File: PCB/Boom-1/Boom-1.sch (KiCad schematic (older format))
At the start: 702 parts

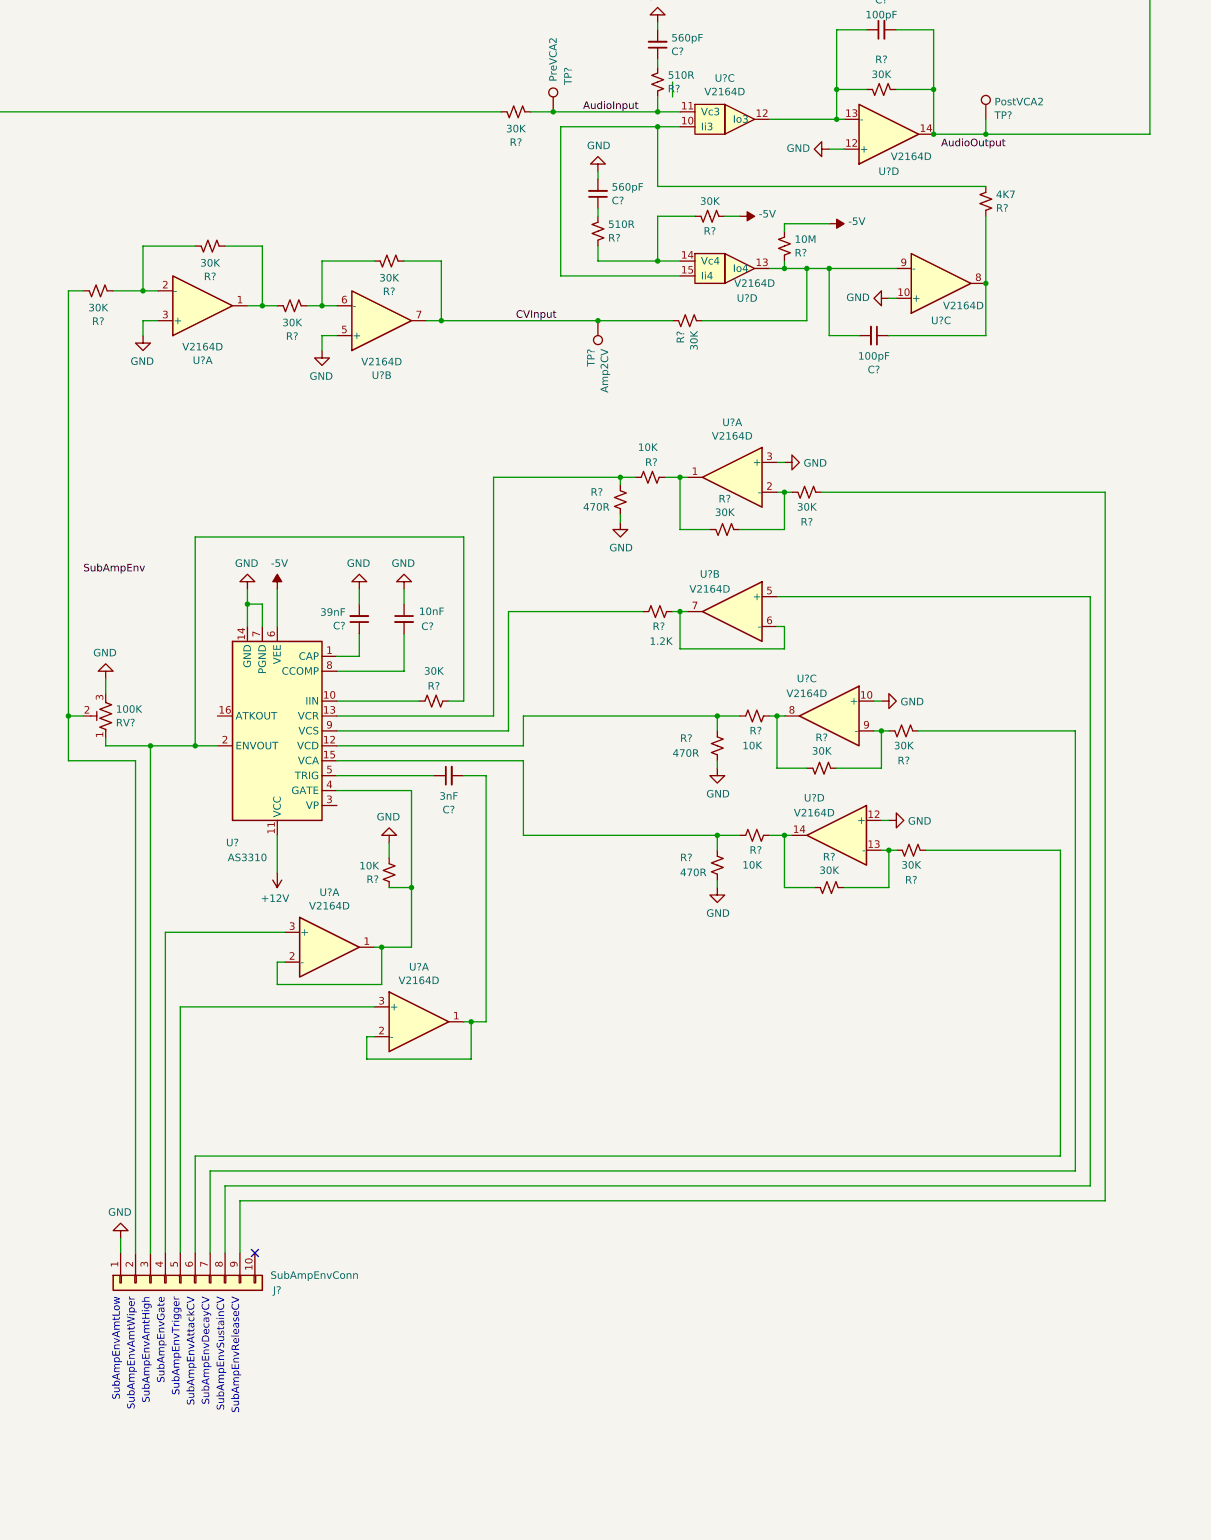
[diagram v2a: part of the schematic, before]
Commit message: replaced tl074 and tl072s in sub osc amp
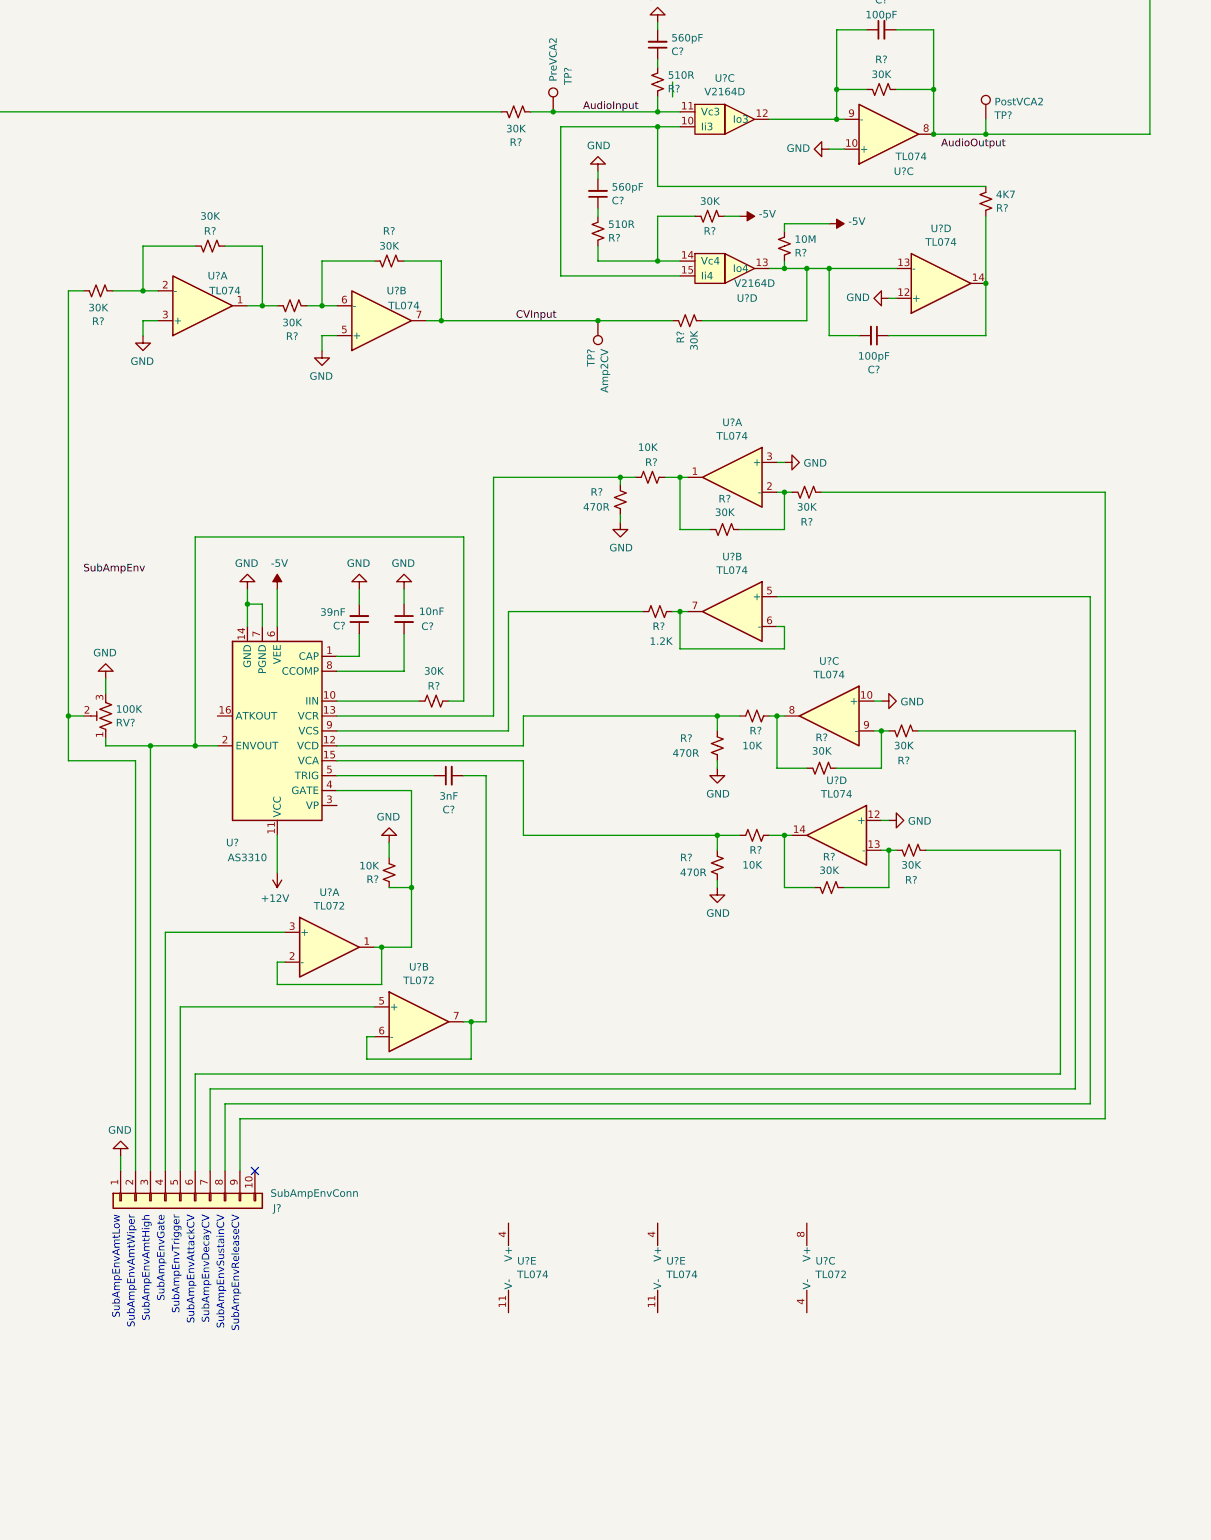
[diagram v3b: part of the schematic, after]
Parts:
- removed U? (x8): V2164D, Package_DIP:DIP-16_W7.62mm_Socket, symbol Amplifier_Operational:TL074
- removed U? (x2): V2164D, Package_DIP:DIP-16_W7.62mm_Socket, symbol Amplifier_Operational:TL072
- added U? (x10): TL074, symbol Amplifier_Operational:TL074
- added U? (x3): TL072, symbol Amplifier_Operational:TL072
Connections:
- net CVInput: now also U?.7
- net GND: now also U?.10 (+), U?.10 (+), U?.12 (+), U?.12 (+), U?.3 (+), U?.3 (+), U?.5 (+)
- net at R?.1, U?.4 (GATE): now also U?.1, U?.2 (-)
- net at C?.1, R?.1, U?.12 (Io3): now also U?.9 (-)
- net at C?.2, R?.1, R?.2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: now also U?.13 (-)
- net at C?.1, R?.1: now also U?.14
- net at C?.2, R?.2, R?.2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: now also U?.8
- net at R?.1, R?.2: now also U?.1 (x2)
- net at R?.1, R?.2: now also U?.2 (-)
- net at R?.1, R?.2: now also U?.6 (-)
- net at C?.2: now also U?.6 (-), U?.7
- net at J?.4 (Pin_4): now also U?.3 (+)
- net at J?.5 (Pin_5): now also U?.5 (+)
- net at J?.8 (Pin_8): now also U?.5 (+)
- net at R?.2: now also U?.6 (-), U?.7
- net at R?.2, R?.2: now also U?.2 (-)
- net at R?.1, R?.2: now also U?.8
- net at R?.2, R?.2: now also U?.9 (-)
- net at R?.1, R?.2: now also U?.14
- net at R?.2, R?.2: now also U?.13 (-)
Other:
- moved on the sheet: J?

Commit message: replaced NOISE, TL074 and V2164D in Noise section - Everything looks good - Power units all dropped - No errors on svae - Symbols all have correct values
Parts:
- removed U? (x4): V2164D, Package_DIP:DIP-16_W7.62mm_Socket, symbol Amplifier_Operational:TL074
- removed U?: V2164D, Package_DIP:DIP-16_W7.62mm_Socket, symbol CustomSymbols:NOISE
- removed U? (x2): V2164D, Package_DIP:DIP-16_W7.62mm_Socket, symbol CustomSymbols:V2164D
- added U?: NOISE, symbol CustomSymbols:NOISE
- added U? (x3): V2164D, Package_DIP:DIP-16_W7.62mm_Socket, symbol CustomSymbols:V2164D
- added U? (x5): TL074, symbol Amplifier_Operational:TL074
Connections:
- net +5V: now also U?.1 (+5V)
- net GND: now also U?.10 (+), U?.12 (+), U?.8 (GND)
- net at J?.2 (Pin_2), R?.2, R?.2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: now also U?.8
- net at R?.1, R?.1: now also U?.9 (-)
- net at R?.1, R?.2: now also U?.13 (-)
- net at J?.1 (Pin_1), R?.2, TP?.1: now also U?.14
- net at R?.2: now also U?.3 (WhiteNoise)
- net at R?.1, R?.1: now also U?.2 (Ii1)
- net at R?.1, R?.1: now also U?.7 (Ii2)
- net at C?.1, R?.2, U?.13 (Io4)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: now also U?.4 (Io1)
- net at R?.2: now also U?.7 (PinkNoise)
- net at C?.1, R?.2, U?.2 (-)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: now also U?.5 (Io2)
- net at R?.1, TP?.1: now also U?.3 (Vc1)
- net at R?.1, TP?.1: now also U?.6 (Vc2)
- net at R?.2, R?.2: now also U?.7
- net at R?.2, R?.2: now also U?.1
- net at R?.1, R?.2: now also U?.2 (-)
- net at R?.2, R?.2: now also U?.3 (+)
- net at R?.1, R?.2: now also U?.6 (-)
- net at R?.2, R?.2: now also U?.5 (+)
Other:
- moved on the sheet: C?, R?, U?C
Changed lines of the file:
@@
 L Device:R_Small_US R?
 U 1 1 60468975
-P 13850 8300
-F 0 "R?" V 13645 8300 50  0000 C CNN
-F 1 "30K" V 13736 8300 50  0000 C CNN
-F 2 "" H 13850 8300 50  0001 C CNN
-F 3 "~" H 13850 8300 50  0001 C CNN
-	1    13850 8300
+P 17050 8300
+F 0 "R?" V 16845 8300 50  0000 C CNN
+F 1 "30K" V 16936 8300 50  0000 C CNN
+F 2 "" H 17050 8300 50  0001 C CNN
+F 3 "~" H 17050 8300 50  0001 C CNN
+	1    17050 8300
 	0    1    1    0
 $EndComp
 Wire Wire Line
-	14100 7950 14100 8300
+	17300 7950 17300 8300
 Wire Wire Line
-	14100 8300 13950 8300
+	17300 8300 17150 8300
 Wire Wire Line
-	13750 8300 13450 8300
+	16950 8300 16650 8300
 Wire Wire Line
-	13450 8300 13450 8050
-Connection ~ 13450 8050
+	16650 8300 16650 8050
+Connection ~ 16650 8050
 Wire Wire Line
-	13450 8050 13500 8050
+	16650 8050 16700 8050
 $Comp
 L Device:C_Small C?
 U 1 1 60468981
-P 13850 8650
-F 0 "C?" V 13621 8650 50  0000 C CNN
-F 1 "100pF" V 13712 8650 50  0000 C CNN
-F 2 "" H 13850 8650 50  0001 C CNN
-F 3 "~" H 13850 8650 50  0001 C CNN
-	1    13850 8650
+P 17050 8650
+F 0 "C?" V 16821 8650 50  0000 C CNN
+F 1 "100pF" V 16912 8650 50  0000 C CNN
+F 2 "" H 17050 8650 50  0001 C CNN
+F 3 "~" H 17050 8650 50  0001 C CNN
+	1    17050 8650
 	0    -1   1    0
 $EndComp
 Wire Wire Line
-	13450 8300 13450 8650
+	16650 8300 16650 8650
 Wire Wire Line
-	13450 8650 13750 8650
-Connection ~ 13450 8300
+	16650 8650 16950 8650
+Connection ~ 16650 8300
 Wire Wire Line
-	14100 8300 14100 8650
+	17300 8300 17300 8650
 Wire Wire Line
-	14100 8650 13950 8650
-Connection ~ 14100 8300
+	17300 8650 17150 8650
+Connection ~ 17300 8300
 $Comp
 L power:GND #PWR?
 U 1 1 6046898D
-P 13450 7850
-F 0 "#PWR?" H 13450 7600 50  0001 C CNN
-F 1 "GND" V 13455 7722 50  0000 R CNN
-F 2 "" H 13450 7850 50  0001 C CNN
-F 3 "" H 13450 7850 50  0001 C CNN
-	1    13450 7850
+P 16650 7850
+F 0 "#PWR?" H 16650 7600 50  0001 C CNN
+F 1 "GND" V 16655 7722 50  0000 R CNN
+F 2 "" H 16650 7850 50  0001 C CNN
+F 3 "" H 16650 7850 50  0001 C CNN
+	1    16650 7850
 	0    1    1    0
 $EndComp
 Wire Wire Line
-	13500 7850 13450 7850
+	16700 7850 16650 7850
 Wire Wire Line
 	18100 38200 18050 38200
@@
 	12550 9150 13500 9150
 Wire Wire Line
-	12600 8050 13450 8050
+	12600 8050 16650 8050
 Wire Wire Line
 	26800 26300 26800 26500
@@
 Wire Wire Line
 	13850 46450 13850 38400
-$Comp
-L Amplifier_Operational:TL074 U?
-U 2 1 5EA64782
-P 7100 46500
-F 0 "U?" H 7100 46867 50  0000 C CNN
-F 1 "V2164D" H 7100 46776 50  0000 C CNN
-F 2 "Package_DIP:DIP-16_W7.62mm_Socket" H 7050 46600 50  0001 C CNN
-F 3 "" H 7150 46700 50  0001 C CNN
-	2    7100 46500
-	1    0    0    -1
-$EndComp
 Wire Wire Line
 	5300 39450 5400 39450
@@
 	15250 5750 14950 5750
 Wire Wire Line
-	14100 7950 18650 7950
+	17300 7950 18650 7950
 Wire Wire Line
 	22750 7950 22750 8450
@@
 $EndComp
 $Comp
-L CustomSymbols:V2164D U?
-U 2 1 600FF1FF
-P 12700 46450
-F 0 "U?" H 12700 46725 50  0000 C CNN
-F 1 "V2164D" H 12700 46634 50  0000 C CNN
-F 2 "Package_DIP:DIP-16_W7.62mm_Socket" H 13450 46200 50  0001 C CNN
-F 3 "" H 12750 46600 50  0001 C CNN
-	2    12700 46450
-	1    0    0    -1
-$EndComp
-$Comp
-L Amplifier_Operational:TL074 U?
-U 1 1 5EA62AE2
-P 7100 44950
-F 0 "U?" H 7100 45317 50  0000 C CNN
-F 1 "V2164D" H 7100 45226 50  0000 C CNN
-F 2 "Package_DIP:DIP-16_W7.62mm_Socket" H 7050 45050 50  0001 C CNN
-F 3 "" H 7150 45150 50  0001 C CNN
-	1    7100 44950
-	1    0    0    -1
-$EndComp
-$Comp
-L CustomSymbols:NOISE U?
-U 1 1 5FEFBD4F
-P 4200 45900
-F 0 "U?" H 4200 46365 50  0000 C CNN
-F 1 "V2164D" H 4200 46274 50  0000 C CNN
-F 2 "Package_DIP:DIP-16_W7.62mm_Socket" H 4000 46350 50  0001 C CNN
-F 3 "" H 4000 46350 50  0001 C CNN
-	1    4200 45900
-	1    0    0    -1
-$EndComp
-$Comp
-L Amplifier_Operational:TL074 U?
-U 1 1 770F3691
-P 9550 44100
-F 0 "U?" H 9550 44467 50  0000 C CNN
-F 1 "V2164D" H 9550 44376 50  0000 C CNN
-F 2 "Package_DIP:DIP-16_W7.62mm_Socket" H 9500 44200 50  0001 C CNN
-F 3 "" H 9600 44300 50  0001 C CNN
-	1    9550 44100
-	1    0    0    -1
-$EndComp
-$Comp
-L Amplifier_Operational:TL074 U?
-U 1 1 770F3594
-P 10550 43150
-F 0 "U?" H 10550 43517 50  0000 C CNN
-F 1 "V2164D" H 10550 43426 50  0000 C CNN
-F 2 "Package_DIP:DIP-16_W7.62mm_Socket" H 10500 43250 50  0001 C CNN
-F 3 "" H 10600 43350 50  0001 C CNN
-	1    10550 43150
-	1    0    0    -1
-$EndComp
-$Comp
 L Regulator_Linear:LM7805_TO220 U?
 U 1 1 B3F23F0A
@@
 $Comp
 L CustomSymbols:V2164D U?
-U 1 1 600F8428
-P 12700 44900
-F 0 "U?" H 12700 45175 50  0000 C CNN
-F 1 "V2164D" H 12700 45084 50  0000 C CNN
-F 2 "Package_DIP:DIP-16_W7.62mm_Socket" H 13450 44650 50  0001 C CNN
-F 3 "" H 12750 45050 50  0001 C CNN
-	1    12700 44900
-	1    0    0    -1
-$EndComp
-$Comp
-L CustomSymbols:V2164D U?
 U 3 1 60105F5D
 P 30850 25250
@@
 L Amplifier_Operational:TL074 U?
 U 3 1 6012C079
-P 13800 7950
-F 0 "U?" H 13800 8317 50  0000 C CNN
-F 1 "TL074" H 13800 8226 50  0000 C CNN
-F 2 "" H 13750 8050 50  0001 C CNN
-F 3 "http://www.ti.com/lit/ds/symlink/tl071.pdf" H 13850 8150 50  0001 C CNN
-	3    13800 7950
+P 17000 7950
+F 0 "U?" H 17000 8317 50  0000 C CNN
+F 1 "TL074" H 17000 8226 50  0000 C CNN
+F 2 "" H 16950 8050 50  0001 C CNN
+F 3 "http://www.ti.com/lit/ds/symlink/tl071.pdf" H 17050 8150 50  0001 C CNN
+	3    17000 7950
 	1    0    0    -1
 $EndComp
-Connection ~ 14100 7950
+Connection ~ 17300 7950
 $Comp
 L Amplifier_Operational:TL074 U?
@@
 	1    0    0    -1
 $EndComp
+$Comp
+L CustomSymbols:NOISE U?
+U 1 1 69EFCD82
+P 4200 45900
+F 0 "U?" H 4200 46365 50  0000 C CNN
+F 1 "NOISE" H 4200 46274 50  0000 C CNN
+F 2 "" H 4000 46350 50  0001 C CNN
+F 3 "" H 4000 46350 50  0001 C CNN
+	1    4200 45900
+	1    0    0    -1
+$EndComp
+$Comp
+L CustomSymbols:V2164D U?
+U 1 1 69F042B2
+P 12700 44900
+F 0 "U?" H 12700 45175 50  0000 C CNN
+F 1 "V2164D" H 12700 45084 50  0000 C CNN
+F 2 "Package_DIP:DIP-16_W7.62mm_Socket" H 13450 44650 50  0001 C CNN
+F 3 "" H 12750 45050 50  0001 C CNN
+	1    12700 44900
+	1    0    0    -1
+$EndComp
+$Comp
+L CustomSymbols:V2164D U?
+U 2 1 69F0C060
+P 12700 46450
+F 0 "U?" H 12700 46725 50  0000 C CNN
+F 1 "V2164D" H 12700 46634 50  0000 C CNN
+F 2 "Package_DIP:DIP-16_W7.62mm_Socket" H 13450 46200 50  0001 C CNN
+F 3 "" H 12750 46600 50  0001 C CNN
+	2    12700 46450
+	1    0    0    -1
+$EndComp
+$Comp
+L Amplifier_Operational:TL074 U?
+U 1 1 69F139BD
+P 10550 43150
+F 0 "U?" H 10550 43517 50  0000 C CNN
+F 1 "TL074" H 10550 43426 50  0000 C CNN
+F 2 "" H 10500 43250 50  0001 C CNN
+F 3 "http://www.ti.com/lit/ds/symlink/tl071.pdf" H 10600 43350 50  0001 C CNN
+	1    10550 43150
+	1    0    0    -1
+$EndComp
+$Comp
+L Amplifier_Operational:TL074 U?
+U 2 1 69F1B5EF
+P 9550 44100
+F 0 "U?" H 9550 44467 50  0000 C CNN
+F 1 "TL074" H 9550 44376 50  0000 C CNN
+F 2 "" H 9500 44200 50  0001 C CNN
+F 3 "http://www.ti.com/lit/ds/symlink/tl071.pdf" H 9600 44300 50  0001 C CNN
+	2    9550 44100
+	1    0    0    -1
+$EndComp
+$Comp
+L Amplifier_Operational:TL074 U?
+U 3 1 69F235EB
+P 7100 44950
+F 0 "U?" H 7100 45317 50  0000 C CNN
+F 1 "TL074" H 7100 45226 50  0000 C CNN
+F 2 "" H 7050 45050 50  0001 C CNN
+F 3 "http://www.ti.com/lit/ds/symlink/tl071.pdf" H 7150 45150 50  0001 C CNN
+	3    7100 44950
+	1    0    0    -1
+$EndComp
+$Comp
+L Amplifier_Operational:TL074 U?
+U 4 1 69F2BE9E
+P 7100 46500
+F 0 "U?" H 7100 46867 50  0000 C CNN
+F 1 "TL074" H 7100 46776 50  0000 C CNN
+F 2 "" H 7050 46600 50  0001 C CNN
+F 3 "http://www.ti.com/lit/ds/symlink/tl071.pdf" H 7150 46700 50  0001 C CNN
+	4    7100 46500
+	1    0    0    -1
+$EndComp
+$Comp
+L Amplifier_Operational:TL074 U?
+U 5 1 69F33B8D
+P 9100 48300
+F 0 "U?" H 9058 48346 50  0000 L CNN
+F 1 "TL074" H 9058 48255 50  0000 L CNN
+F 2 "" H 9050 48400 50  0001 C CNN
+F 3 "http://www.ti.com/lit/ds/symlink/tl071.pdf" H 9150 48500 50  0001 C CNN
+	5    9100 48300
+	1    0    0    -1
+$EndComp
+$Comp
+L CustomSymbols:V2164D U?
+U 5 1 69F3E5A0
+P 10150 48250
+F 0 "U?" H 10108 48271 50  0000 L CNN
+F 1 "V2164D" H 10108 48180 50  0000 L CNN
+F 2 "Package_DIP:DIP-16_W7.62mm_Socket" H 10900 48000 50  0001 C CNN
+F 3 "" H 10200 48400 50  0001 C CNN
+	5    10150 48250
+	1    0    0    -1
+$EndComp

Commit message: note about power
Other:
- note added: "Power for both envelopes"
- moved on the sheet: U?E
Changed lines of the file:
@@
 L Amplifier_Operational:TL074 U?
 U 5 1 6917B785
-P 21350 49150
-F 0 "U?" H 21308 49196 50  0000 L CNN
-F 1 "TL074" H 21308 49105 50  0000 L CNN
-F 2 "" H 21300 49250 50  0001 C CNN
-F 3 "http://www.ti.com/lit/ds/symlink/tl071.pdf" H 21400 49350 50  0001 C CNN
-	5    21350 49150
+P 22150 49150
+F 0 "U?" H 22108 49196 50  0000 L CNN
+F 1 "TL074" H 22108 49105 50  0000 L CNN
+F 2 "" H 22100 49250 50  0001 C CNN
+F 3 "http://www.ti.com/lit/ds/symlink/tl071.pdf" H 22200 49350 50  0001 C CNN
+	5    22150 49150
 	1    0    0    -1
 $EndComp
@@
 L Amplifier_Operational:TL074 U?
 U 5 1 69181953
-P 22350 49150
-F 0 "U?" H 22308 49196 50  0000 L CNN
-F 1 "TL074" H 22308 49105 50  0000 L CNN
-F 2 "" H 22300 49250 50  0001 C CNN
-F 3 "http://www.ti.com/lit/ds/symlink/tl071.pdf" H 22400 49350 50  0001 C CNN
-	5    22350 49150
+P 23150 49150
+F 0 "U?" H 23108 49196 50  0000 L CNN
+F 1 "TL074" H 23108 49105 50  0000 L CNN
+F 2 "" H 23100 49250 50  0001 C CNN
+F 3 "http://www.ti.com/lit/ds/symlink/tl071.pdf" H 23200 49350 50  0001 C CNN
+	5    23150 49150
 	1    0    0    -1
 $EndComp
@@
 L Amplifier_Operational:TL074 U?
 U 5 1 69183854
-P 23350 49150
-F 0 "U?" H 23308 49196 50  0000 L CNN
-F 1 "TL074" H 23308 49105 50  0000 L CNN
-F 2 "" H 23300 49250 50  0001 C CNN
-F 3 "http://www.ti.com/lit/ds/symlink/tl071.pdf" H 23400 49350 50  0001 C CNN
-	5    23350 49150
+P 24150 49150
+F 0 "U?" H 24108 49196 50  0000 L CNN
+F 1 "TL074" H 24108 49105 50  0000 L CNN
+F 2 "" H 24100 49250 50  0001 C CNN
+F 3 "http://www.ti.com/lit/ds/symlink/tl071.pdf" H 24200 49350 50  0001 C CNN
+	5    24150 49150
 	1    0    0    -1
 $EndComp
@@
 	1    0    0    -1
 $EndComp
+Text Notes 20700 49200 0    50   ~ 0
+Power for both envelopes
 $EndSCHEMATC
